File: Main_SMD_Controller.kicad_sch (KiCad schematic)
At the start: 65 parts, among them J1 2.1-5.5 +12VDC, J10 Vin_-, J11 Conn_01x02, J12 Vsens, J13 Vin+, J2 Switch_Control, J3 +5V, J4 AnalogIO, J5 +12V, J6 VsensJMP, J7 Drain, J8 Gate, J9 Source, P1 Eoshi-chan_Silk, P2 Eoshi-chan_Silk, P3 Serial_QR, Q1 2N7002K, U1 NJW4191M, U2 NJM7805SDL1, U3 TC74HC4066AP, U4 AD8226ARZ, U5 S-89713B-K8T2U, U6 S-89713B-K8T2U

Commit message: bom and schematic pdf
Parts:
- added C13: 1u, Capacitor_SMD:C_0603_1608Metric, symbol Device:C_Small
- added R18: 10k, Resistor_SMD:R_0603_1608Metric, symbol Device:R
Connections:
- net GND: now also C13.2
- net VEE: now also C13.1, R18.2; no longer C6.1, R1.2, U1.5 (Vout)
- new net: C6.1, R1.2, R18.1, U1.5 (Vout)

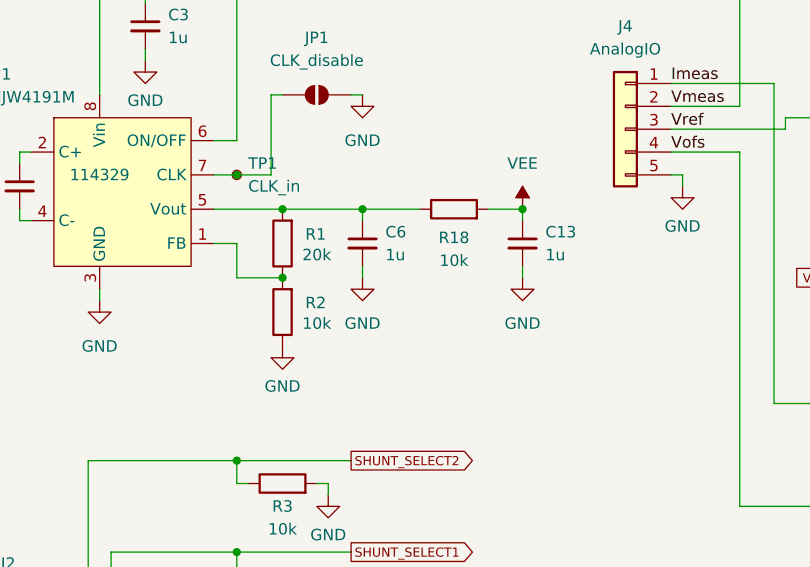
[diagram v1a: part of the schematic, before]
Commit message: Update Main_SMD_Controller.kicad_sch
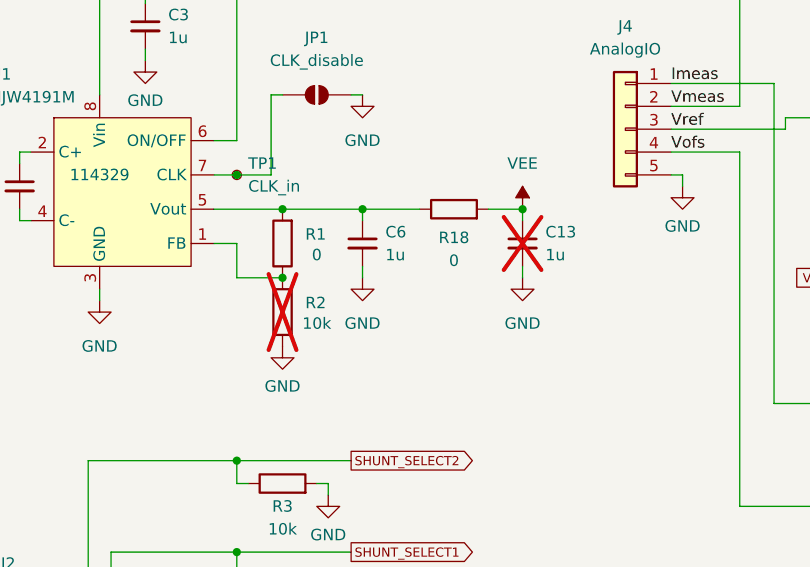
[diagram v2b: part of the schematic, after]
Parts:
- C13, R2: now not fitted
- R1: value 20k -> 0
- R18: value 10k -> 0
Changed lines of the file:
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@@
 			)
 		)
-		(property "Value" "10k"
+		(property "Value" "0"
 			(at 85.09 95.885 90)
 			(effects
@@
 		(in_bom yes)
 		(on_board yes)
-		(dnp no)
+		(dnp yes)
 		(property "Reference" "R2"
 			(at 69.723 100.584 0)
@@
 			)
 		)
-		(property "Value" "20k"
+		(property "Value" "0"
 			(at 69.85 95.25 0)
 			(effects
@@
 		(in_bom yes)
 		(on_board yes)
-		(dnp no)
+		(dnp yes)
 		(fields_autoplaced yes)
 		(property "Reference" "C13"

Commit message: add v2 version
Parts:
- removed R17, R7: 10k, Resistor_SMD:R_0603_1608Metric, symbol Device:R
- removed U5, U6: S-89713B-K8T2U, Package_SO:MSOP-8_3x3mm_P0.65mm, symbol dk_Linear-Amplifiers-Instrumentation-OP-Amps-Buffer-Amps:LM358N_Obsolete
- added U5: ADA4522-1, Package_SO:SOIC-8_3.9x4.9mm_P1.27mm, symbol Amplifier_Operational:ADA4522-1
- added U6: ADA4075-2, Package_SO:SOIC-8_3.9x4.9mm_P1.27mm, symbol Amplifier_Operational:ADA4075-2
- added U7: 74AHC1G04, Package_TO_SOT_SMD:SOT-23-5, symbol 74xGxx:74AHC1G04
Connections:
- net +12V: now also C3.1, U1.6 (ON/OFF), U1.8 (Vin), U4.8 (Vs+), U5.7 (VCC), U6.8 (VCC), U6.8 (VCC)
- net GND: now also U7.3 (GND); no longer U3.12
- net VCC: now also U7.5 (VCC); no longer C3.1, U1.6 (ON/OFF), U1.8 (Vin), U4.8 (Vs+)
- net VEE: no longer C13.1, R18.2, U4.5 (Vs-)
- net Vconst_ENABLE: now also U7.2
- net Vmeas: now also U3.10, U6.7
- net Vref: now also U5.3
- net at R13.1, R14.1: now also U6.5
- net at R13.2: now also U6.1, U6.2
- net at R15.1, R16.2: now also U6.6
- net at R10.1, R8.2: now also U6.3
- net at U3.11: now also RV1.3, U3.9
- net at C12.2, R9.1: now also U5.6
- net at C12.1, RV1.1, RV1.2: now also U5.2
- new net -12V: C13.1, R18.2, U4.5 (Vs-), U5.4 (VEE), U6.4 (VEE), U6.4 (VEE)
- new net nVconst_ENABLE: U3.12, U7.4
- no-connect marks 3 -> 1
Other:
- note removed: "(Vofs+0)~(Vofs+2.048)V (Vofs=2)"
- moved on the sheet: C12, R15, R16, U3D
